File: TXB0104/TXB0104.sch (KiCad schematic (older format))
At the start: 6 parts, among them J1 Conn_01x06, J2 Conn_01x06, U1 TXB0104D

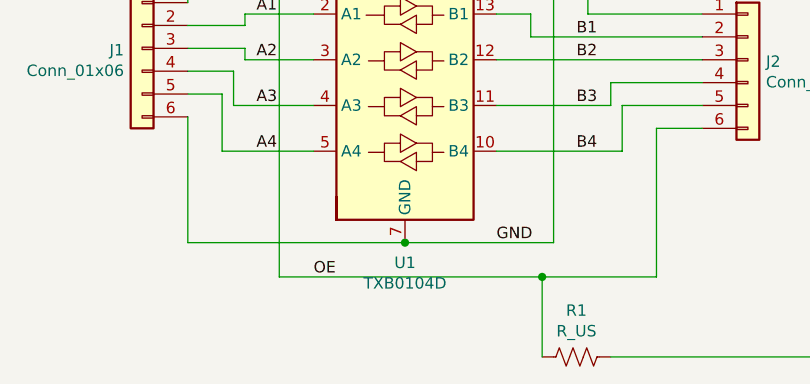
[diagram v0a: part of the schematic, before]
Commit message: SOIC8 Changed to TSSOP8
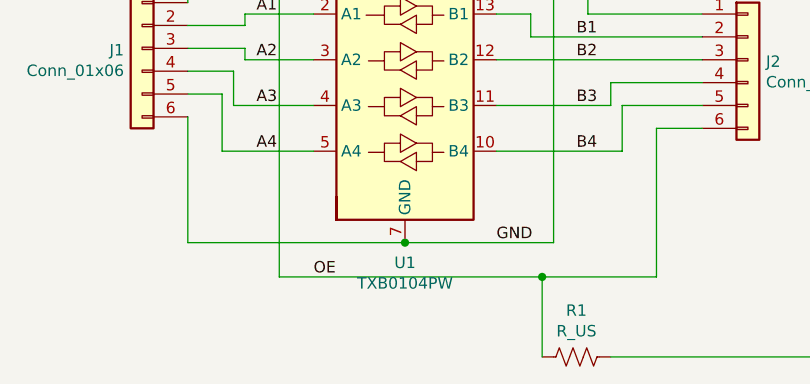
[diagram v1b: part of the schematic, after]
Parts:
- removed U1: TXB0104D, Package_SO:SOIC-14_3.9x8.7mm_P1.27mm, symbol Logic_LevelTranslator:TXB0104D
- added U1: TXB0104PW, Package_SO:TSSOP-14_4.4x5mm_P0.65mm, symbol Logic_LevelTranslator:TXB0104PW
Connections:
- net A1: now also U1.2 (A1)
- net A2: now also U1.3 (A2)
- net A3: now also U1.4 (A3)
- net A4: now also U1.5 (A4)
- net B1: now also U1.13 (B1)
- net B2: now also U1.12 (B2)
- net B3: now also U1.11 (B3)
- net B4: now also U1.10 (B4)
- net GND: now also U1.7 (GND)
- net OE: now also U1.8 (OE)
- net VHI: now also U1.14 (VCCB)
- net VLOW: now also U1.1 (VCCA)
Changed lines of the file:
@@
 EESchema Schematic File Version 4
+LIBS:TXB0104-cache
 EELAYER 29 0
 EELAYER END
@@
 $EndDescr
 $Comp
-L Logic_LevelTranslator:TXB0104D U1
-U 1 1 5D2E48EB
-P 5500 3700
-F 0 "U1" H 5500 2912 50  0000 C CNN
-F 1 "TXB0104D" H 5500 2822 50  0000 C CNN
-F 2 "Package_SO:SOIC-14_3.9x8.7mm_P1.27mm" H 5500 2950 50  0001 C CNN
-F 3 "http://www.ti.com/lit/ds/symlink/txb0104.pdf" H 5610 3795 50  0001 C CNN
-	1    5500 3700
-	1    0    0    -1
-$EndComp
-$Comp
 L Device:C C2
 U 1 1 5D2E53A3
@@
 	5600 2350 5600 2450
 Wire Wire Line
-	5500 4400 6150 4400
-Wire Wire Line
 	6150 4400 6150 2350
 Wire Wire Line
@@
 Wire Wire Line
 	4700 4000 5100 4000
-Wire Wire Line
-	4550 3850 4550 4400
-Wire Wire Line
-	4550 4400 5500 4400
-Connection ~ 5500 4400
 Wire Wire Line
 	5100 3200 4950 3200
@@
 Wire Wire Line
 	5400 2800 5400 2750
+$Comp
+L Logic_LevelTranslator:TXB0104PW U1
+U 1 1 5D8F47CC
+P 5500 3700
+F 0 "U1" H 5500 2912 50  0000 C CNN
+F 1 "TXB0104PW" H 5500 2822 50  0000 C CNN
+F 2 "Package_SO:TSSOP-14_4.4x5mm_P0.65mm" H 5500 2950 50  0001 C CNN
+F 3 "http://www.ti.com/lit/ds/symlink/txb0104.pdf" H 5610 3795 50  0001 C CNN
+	1    5500 3700
+	1    0    0    -1
+$EndComp
+Wire Wire Line
+	4550 4400 5500 4400
+Connection ~ 5500 4400
+Wire Wire Line
+	5500 4400 6150 4400
+Wire Wire Line
+	4550 3850 4550 4400
 $EndSCHEMATC

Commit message: Silkscreen Updated
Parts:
- R1: value R_US -> 4K7
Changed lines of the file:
@@
 P 6250 4900
 F 0 "R1" V 6047 4900 50  0000 C CNN
-F 1 "R_US" V 6137 4900 50  0000 C CNN
+F 1 "4K7" V 6137 4900 50  0000 C CNN
 F 2 "Resistor_SMD:R_0805_2012Metric_Pad1.15x1.40mm_HandSolder" V 6290 4890 50  0001 C CNN
 F 3 "~" H 6250 4900 50  0001 C CNN

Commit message: Part Numbers Added
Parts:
- C1, C2: Part (none) -> C38141
- R1: Part (none) -> C99782
- U1: Part (none) -> C60708
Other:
- moved on the sheet: C1, C2, J1, J2, R1, U1
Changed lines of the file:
@@
 EELAYER 29 0
 EELAYER END
-$Descr A4 11693 8268
+$Descr User 8268 5807
 encoding utf-8
 Sheet 1 1
-Title ""
-Date ""
-Rev ""
-Comp ""
-Comment1 ""
-Comment2 ""
-Comment3 ""
+Title "4 Channel Bi-Directional Level Shifter"
+Date "2019-09-16"
+Rev "1"
+Comp "SirBoard"
+Comment1 "www.SirBoard.com"
+Comment2 "TXB0104"
+Comment3 "SirLevel"
 Comment4 ""
 $EndDescr
@@
 L Device:C C2
 U 1 1 5D2E53A3
-P 5600 2600
-F 0 "C2" H 5715 2645 50  0000 L CNN
-F 1 "100nF" H 5715 2555 50  0000 L CNN
-F 2 "Capacitor_SMD:C_0805_2012Metric_Pad1.15x1.40mm_HandSolder" H 5638 2450 50  0001 C CNN
-F 3 "~" H 5600 2600 50  0001 C CNN
-	1    5600 2600
+P 3675 1375
+F 0 "C2" H 3790 1420 50  0000 L CNN
+F 1 "100nF" H 3790 1330 50  0000 L CNN
+F 2 "Capacitor_SMD:C_0805_2012Metric_Pad1.15x1.40mm_HandSolder" H 3713 1225 50  0001 C CNN
+F 3 "~" H 3675 1375 50  0001 C CNN
+F 4 "C38141" H 3675 1375 50  0001 C CNN "Part"
+	1    3675 1375
 	1    0    0    -1
 $EndComp
@@
 L Device:C C1
 U 1 1 5D2E61B4
-P 5400 2600
-F 0 "C1" H 5515 2645 50  0000 L CNN
-F 1 "100nF" H 5515 2555 50  0000 L CNN
-F 2 "Capacitor_SMD:C_0805_2012Metric_Pad1.15x1.40mm_HandSolder" H 5438 2450 50  0001 C CNN
-F 3 "~" H 5400 2600 50  0001 C CNN
-	1    5400 2600
+P 3475 1375
+F 0 "C1" H 3590 1420 50  0000 L CNN
+F 1 "100nF" H 3590 1330 50  0000 L CNN
+F 2 "Capacitor_SMD:C_0805_2012Metric_Pad1.15x1.40mm_HandSolder" H 3513 1225 50  0001 C CNN
+F 3 "~" H 3475 1375 50  0001 C CNN
+F 4 "C38141" H 3475 1375 50  0001 C CNN "Part"
+	1    3475 1375
 	-1   0    0    -1
 $EndComp
 Wire Wire Line
-	5400 3000 5400 2950
-Wire Wire Line
-	5600 3000 5600 2950
-Wire Wire Line
-	5400 2450 5400 2350
-Wire Wire Line
-	5400 2350 5600 2350
-Wire Wire Line
-	5600 2350 5600 2450
-Wire Wire Line
-	6150 4400 6150 2350
-Wire Wire Line
-	6150 2350 5600 2350
-Connection ~ 5600 2350
+	3475 1775 3475 1725
+Wire Wire Line
+	3675 1775 3675 1725
+Wire Wire Line
+	3475 1225 3475 1125
+Wire Wire Line
+	3475 1125 3675 1125
+Wire Wire Line
+	3675 1125 3675 1225
+Wire Wire Line
+	4225 3175 4225 1125
+Wire Wire Line
+	4225 1125 3675 1125
+Connection ~ 3675 1125
 $Comp
 L Connector_Generic:Conn_01x06 J2
 U 1 1 5D2E7899
-P 7000 3600
-F 0 "J2" H 7079 3592 50  0000 L CNN
-F 1 "Conn_01x06" H 7079 3502 50  0000 L CNN
-F 2 "Connector_PinHeader_2.54mm:PinHeader_1x06_P2.54mm_Vertical" H 7000 3600 50  0001 C CNN
-F 3 "~" H 7000 3600 50  0001 C CNN
-	1    7000 3600
+P 5075 2375
+F 0 "J2" H 5154 2367 50  0000 L CNN
+F 1 "Conn_01x06" H 5154 2277 50  0000 L CNN
+F 2 "Connector_PinHeader_2.54mm:PinHeader_1x06_P2.54mm_Vertical" H 5075 2375 50  0001 C CNN
+F 3 "~" H 5075 2375 50  0001 C CNN
+	1    5075 2375
 	1    0    0    -1
 $EndComp
@@
 L Connector_Generic:Conn_01x06 J1
 U 1 1 5D2E8423
-P 4350 3550
-F 0 "J1" H 4429 3542 50  0000 L CNN
-F 1 "Conn_01x06" H 4429 3452 50  0000 L CNN
-F 2 "Connector_PinHeader_2.54mm:PinHeader_1x06_P2.54mm_Vertical" H 4350 3550 50  0001 C CNN
-F 3 "~" H 4350 3550 50  0001 C CNN
-	1    4350 3550
+P 2425 2325
+F 0 "J1" H 2504 2317 50  0000 L CNN
+F 1 "Conn_01x06" H 2504 2227 50  0000 L CNN
+F 2 "Connector_PinHeader_2.54mm:PinHeader_1x06_P2.54mm_Vertical" H 2425 2325 50  0001 C CNN
+F 3 "~" H 2425 2325 50  0001 C CNN
+	1    2425 2325
 	-1   0    0    -1
 $EndComp
 Wire Wire Line
-	5400 2950 4550 2950
-Wire Wire Line
-	4550 2950 4550 3350
-Connection ~ 5400 2950
-Wire Wire Line
-	5400 2950 5400 2800
-Wire Wire Line
-	4550 3450 4800 3450
-Wire Wire Line
-	4800 3450 4800 3400
-Wire Wire Line
-	4800 3400 5100 3400
-Wire Wire Line
-	4550 3550 4800 3550
-Wire Wire Line
-	4800 3550 4800 3600
-Wire Wire Line
-	4800 3600 5100 3600
-Wire Wire Line
-	4550 3650 4750 3650
-Wire Wire Line
-	4750 3650 4750 3800
-Wire Wire Line
-	4750 3800 5100 3800
-Wire Wire Line
-	4550 3750 4700 3750
-Wire Wire Line
-	4700 3750 4700 4000
-Wire Wire Line
-	4700 4000 5100 4000
-Wire Wire Line
-	5100 3200 4950 3200
-Wire Wire Line
-	4950 3200 4950 4550
-Wire Wire Line
-	4950 4550 6100 4550
-Wire Wire Line
-	6600 4550 6600 3900
-Wire Wire Line
-	6600 3900 6800 3900
-Wire Wire Line
-	5900 4000 6450 4000
-Wire Wire Line
-	6450 4000 6450 3800
-Wire Wire Line
-	6450 3800 6800 3800
-Wire Wire Line
-	5900 3800 6400 3800
-Wire Wire Line
-	6400 3800 6400 3700
-Wire Wire Line
-	6400 3700 6800 3700
-Wire Wire Line
-	5900 3600 6800 3600
-Wire Wire Line
-	6800 3500 6050 3500
-Wire Wire Line
-	6050 3500 6050 3400
-Wire Wire Line
-	6050 3400 5900 3400
-Wire Wire Line
-	6800 3400 6300 3400
-Wire Wire Line
-	6300 3400 6300 2950
-Wire Wire Line
-	6300 2950 5600 2950
-Connection ~ 5600 2950
-Wire Wire Line
-	5600 2950 5600 2750
-Text Label 5900 4400 0    50   ~ 0
+	3475 1725 2625 1725
+Wire Wire Line
+	2625 1725 2625 2125
+Connection ~ 3475 1725
+Wire Wire Line
+	3475 1725 3475 1575
+Wire Wire Line
+	2625 2225 2875 2225
+Wire Wire Line
+	2875 2225 2875 2175
+Wire Wire Line
+	2875 2175 3175 2175
+Wire Wire Line
+	2625 2325 2875 2325
+Wire Wire Line
+	2875 2325 2875 2375
+Wire Wire Line
+	2875 2375 3175 2375
+Wire Wire Line
+	2625 2425 2825 2425
+Wire Wire Line
+	2825 2425 2825 2575
+Wire Wire Line
+	2825 2575 3175 2575
+Wire Wire Line
+	2625 2525 2775 2525
+Wire Wire Line
+	2775 2525 2775 2775
+Wire Wire Line
+	2775 2775 3175 2775
+Wire Wire Line
+	3175 1975 3025 1975
+Wire Wire Line
+	3025 1975 3025 3325
+Wire Wire Line
+	3025 3325 4175 3325
+Wire Wire Line
+	4675 3325 4675 2675
+Wire Wire Line
+	4675 2675 4875 2675
+Wire Wire Line
+	3975 2775 4525 2775
+Wire Wire Line
+	4525 2775 4525 2575
+Wire Wire Line
+	4525 2575 4875 2575
+Wire Wire Line
+	3975 2575 4475 2575
+Wire Wire Line
+	4475 2575 4475 2475
+Wire Wire Line
+	4475 2475 4875 2475
+Wire Wire Line
+	3975 2375 4875 2375
+Wire Wire Line
+	4875 2275 4125 2275
+Wire Wire Line
+	4125 2275 4125 2175
+Wire Wire Line
+	4125 2175 3975 2175
+Wire Wire Line
+	4875 2175 4375 2175
+Wire Wire Line
+	4375 2175 4375 1725
+Wire Wire Line
+	4375 1725 3675 1725
+Connection ~ 3675 1725
+Wire Wire Line
+	3675 1725 3675 1525
+Text Label 3975 3175 0    50   ~ 0
 GND
-Text Label 5950 2950 0    50   ~ 0
+Text Label 4025 1725 0    50   ~ 0
 VHI
-Text Label 4950 2950 0    50   ~ 0
+Text Label 3025 1725 0    50   ~ 0
 VLOW
-Text Label 5100 4550 0    50   ~ 0
+Text Label 3175 3325 0    50   ~ 0
 OE
-Text Label 4850 3400 0    50   ~ 0
+Text Label 2925 2175 0    50   ~ 0
 A1
-Text Label 4850 3600 0    50   ~ 0
+Text Label 2925 2375 0    50   ~ 0
 A2
-Text Label 4850 3800 0    50   ~ 0
+Text Label 2925 2575 0    50   ~ 0
 A3
-Text Label 4850 4000 0    50   ~ 0
+Text Label 2925 2775 0    50   ~ 0
 A4
-Text Label 6250 3500 0    50   ~ 0
+Text Label 4325 2275 0    50   ~ 0
 B1
-Text Label 6250 3600 0    50   ~ 0
+Text Label 4325 2375 0    50   ~ 0
 B2
-Text Label 6250 3800 0    50   ~ 0
+Text Label 4325 2575 0    50   ~ 0
 B3
-Text Label 6250 4000 0    50   ~ 0
+Text Label 4325 2775 0    50   ~ 0
 B4
 $Comp
 L Device:R_US R1
 U 1 1 5D2FAE97
-P 6250 4900
-F 0 "R1" V 6047 4900 50  0000 C CNN
-F 1 "4K7" V 6137 4900 50  0000 C CNN
-F 2 "Resistor_SMD:R_0805_2012Metric_Pad1.15x1.40mm_HandSolder" V 6290 4890 50  0001 C CNN
-F 3 "~" H 6250 4900 50  0001 C CNN
-	1    6250 4900
+P 4325 3675
+F 0 "R1" V 4122 3675 50  0000 C CNN
+F 1 "4K7" V 4212 3675 50  0000 C CNN
+F 2 "Resistor_SMD:R_0805_2012Metric_Pad1.15x1.40mm_HandSolder" V 4365 3665 50  0001 C CNN
+F 3 "~" H 4325 3675 50  0001 C CNN
+F 4 "C99782" V 4325 3675 50  0001 C CNN "Part"
+	1    4325 3675
 	0    1    1    0
 $EndComp
 Wire Wire Line
-	6100 4550 6100 4900
-Wire Wire Line
-	6100 4550 6600 4550
-Connection ~ 6100 4550
-Wire Wire Line
-	6400 4900 7500 4900
-Wire Wire Line
-	7500 4900 7500 2800
-Wire Wire Line
-	7500 2800 5400 2800
-Connection ~ 5400 2800
-Wire Wire Line
-	5400 2800 5400 2750
+	4175 3325 4175 3675
+Wire Wire Line
+	4175 3325 4675 3325
+Connection ~ 4175 3325
+Wire Wire Line
+	4475 3675 5575 3675
+Wire Wire Line
+	5575 3675 5575 1575
+Wire Wire Line
+	5575 1575 3475 1575
+Connection ~ 3475 1575
+Wire Wire Line
+	3475 1575 3475 1525
 $Comp
 L Logic_LevelTranslator:TXB0104PW U1
 U 1 1 5D8F47CC
-P 5500 3700
-F 0 "U1" H 5500 2912 50  0000 C CNN
-F 1 "TXB0104PW" H 5500 2822 50  0000 C CNN
-F 2 "Package_SO:TSSOP-14_4.4x5mm_P0.65mm" H 5500 2950 50  0001 C CNN
-F 3 "http://www.ti.com/lit/ds/symlink/txb0104.pdf" H 5610 3795 50  0001 C CNN
-	1    5500 3700
+P 3575 2475
+F 0 "U1" H 3575 1687 50  0000 C CNN
+F 1 "TXB0104PW" H 3575 1597 50  0000 C CNN
+F 2 "Package_SO:TSSOP-14_4.4x5mm_P0.65mm" H 3575 1725 50  0001 C CNN
+F 3 "http://www.ti.com/lit/ds/symlink/txb0104.pdf" H 3685 2570 50  0001 C CNN
+F 4 "C60708" H 3575 2475 50  0001 C CNN "Part"
+	1    3575 2475
 	1    0    0    -1
 $EndComp
 Wire Wire Line
-	4550 4400 5500 4400
-Connection ~ 5500 4400
-Wire Wire Line
-	5500 4400 6150 4400
-Wire Wire Line
-	4550 3850 4550 4400
+	2625 3175 3575 3175
+Connection ~ 3575 3175
+Wire Wire Line
+	3575 3175 4225 3175
+Wire Wire Line
+	2625 2625 2625 3175
 $EndSCHEMATC
